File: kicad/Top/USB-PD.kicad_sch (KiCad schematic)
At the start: 43 parts

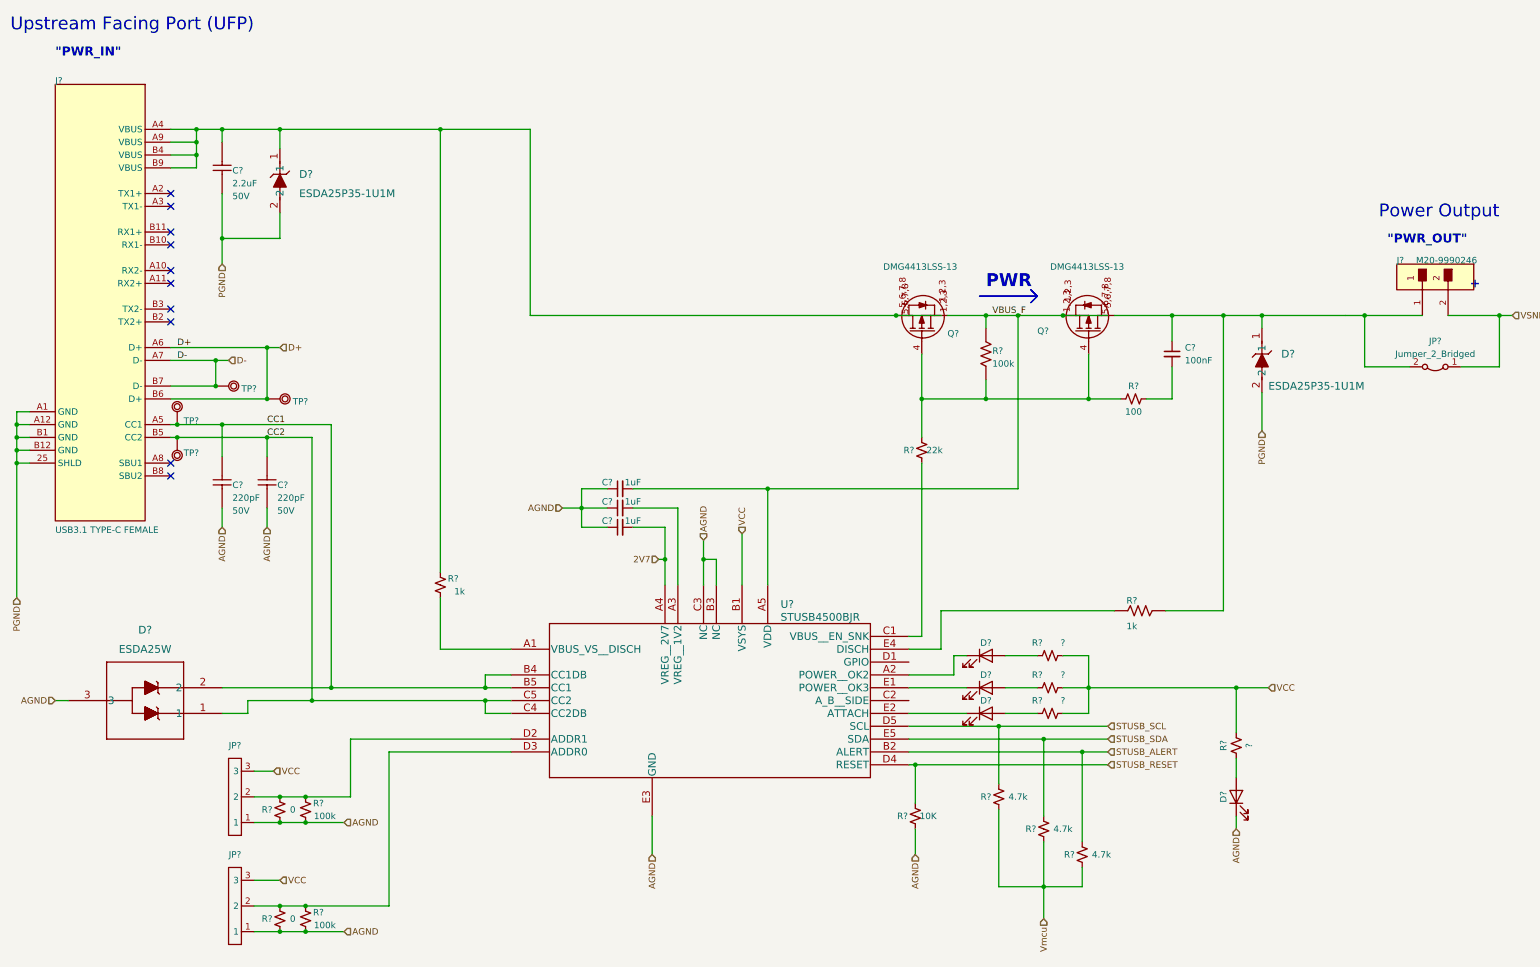
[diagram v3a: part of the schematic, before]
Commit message: Annotated USB-PD schematic
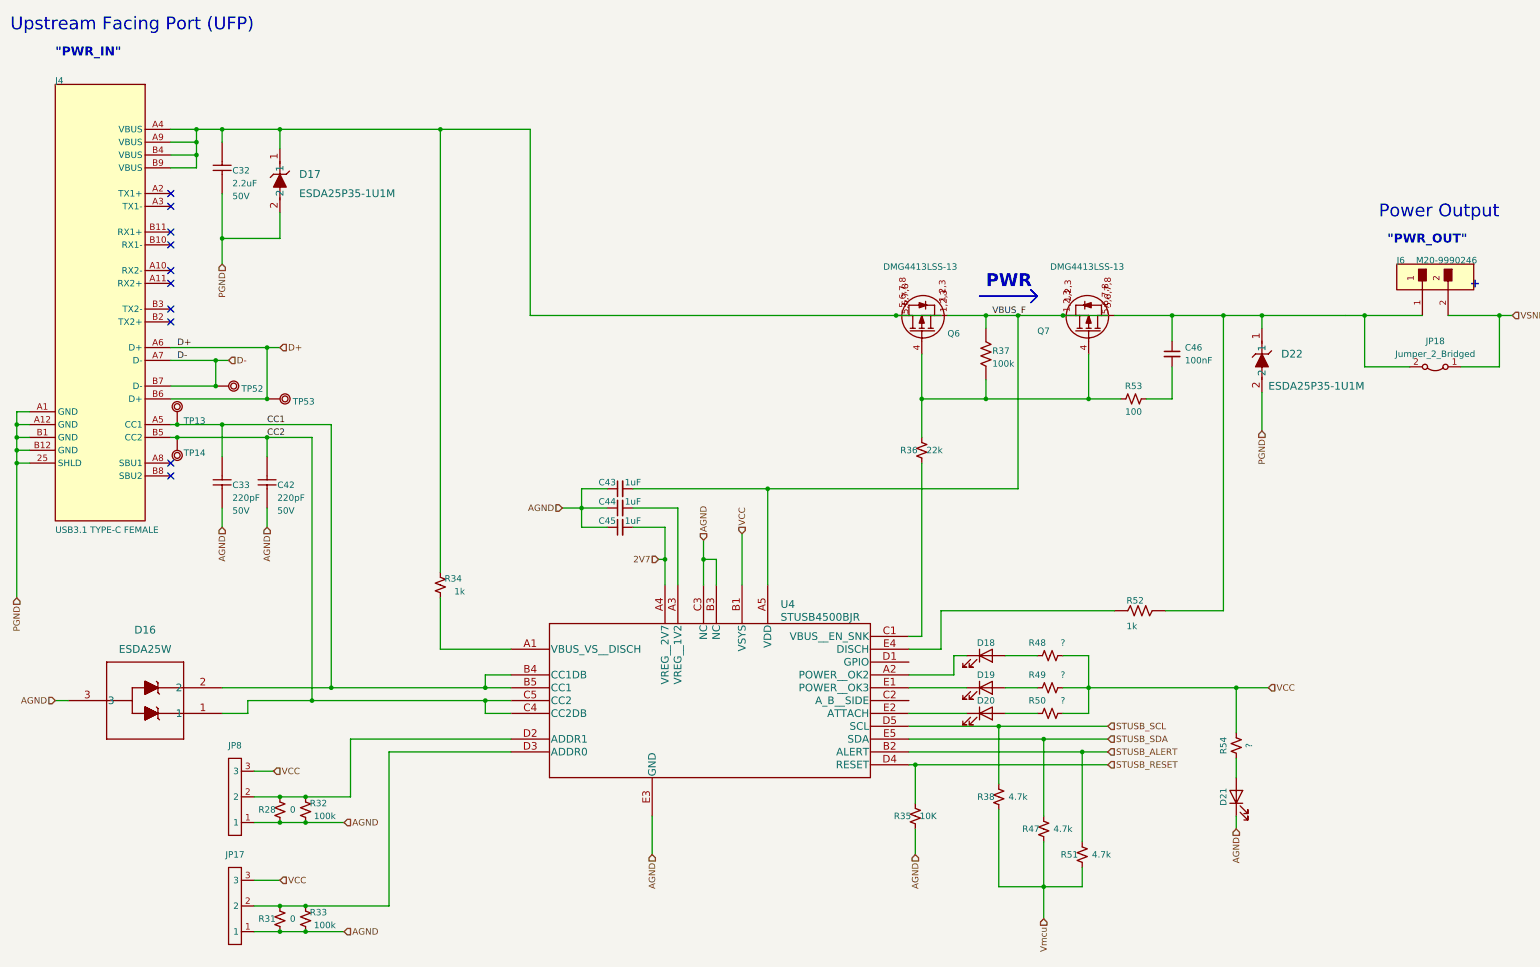
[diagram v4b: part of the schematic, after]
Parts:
- gave numbers to parts that had none: 43

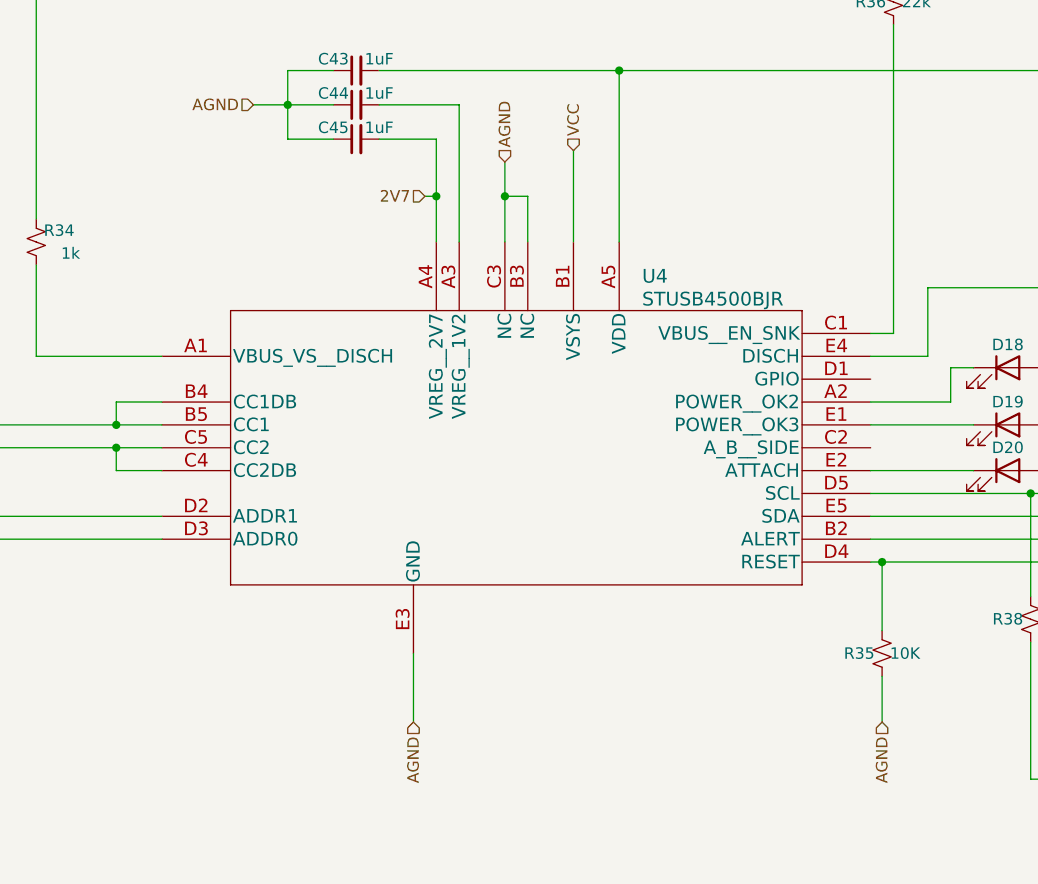
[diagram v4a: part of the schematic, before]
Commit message: Added STUSB4500QTR
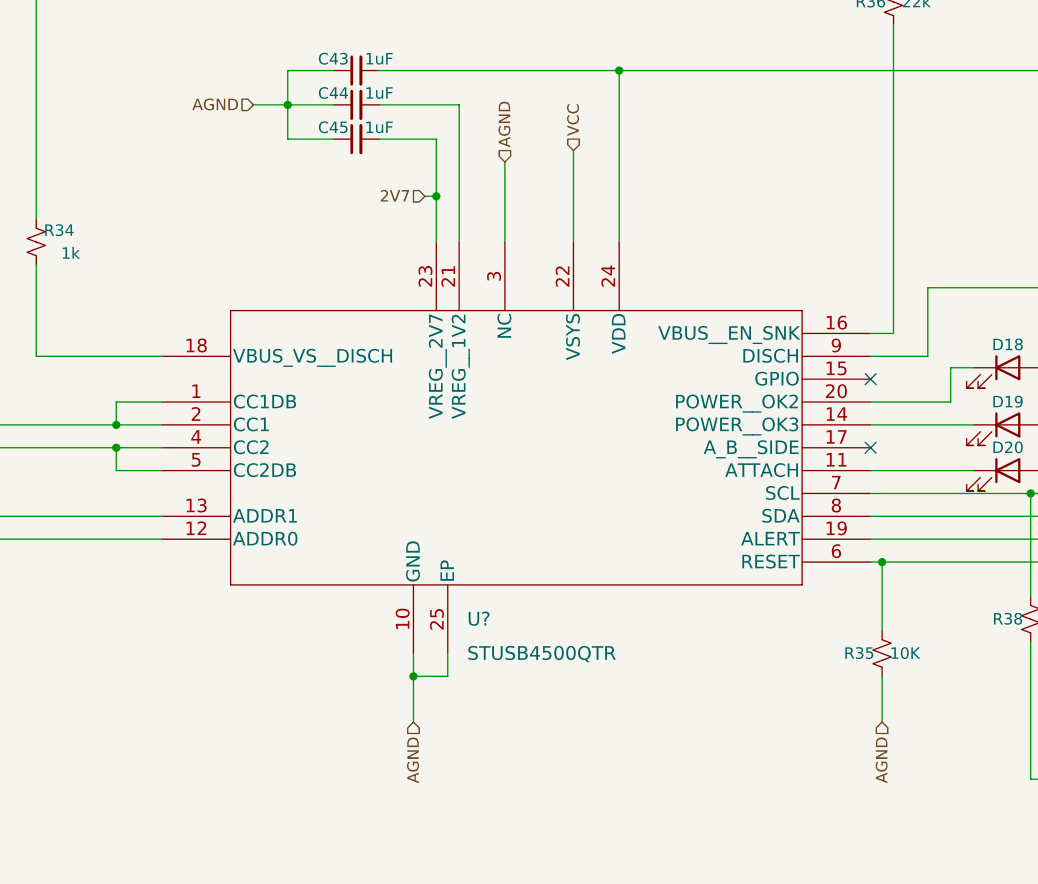
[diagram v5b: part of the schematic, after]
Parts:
- removed U4: STUSB4500BJR, custom_modules:STUSB4500BJR, symbol STUSB4500BJR:STUSB4500BJR
- added U?: STUSB4500QTR, Ultra_Librarian:QFN24EP_4X4_STM, symbol ultralibrarian:STUSB4500QTR
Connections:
- net 2V7: now also U?.23 (VREG__2V7)
- net AGND: now also U?.10 (GND), U?.25 (EP), U?.3 (NC)
- net CC1: now also U?.1 (CC1DB), U?.2 (CC1)
- net CC2: now also U?.4 (CC2), U?.5 (CC2DB)
- net STUSB_ALERT: now also U?.19 (ALERT)
- net STUSB_RESET: now also U?.6 (RESET)
- net STUSB_SCL: now also U?.7 (SCL)
- net STUSB_SDA: now also U?.8 (SDA)
- net VBUS_F: now also U?.24 (VDD)
- net VCC: now also U?.22 (VSYS)
- net at D20.1 (K): now also U?.11 (ATTACH)
- net at R34.2: now also U?.18 (VBUS_VS__DISCH)
- net at JP17.2, R31.1, R33.1: now also U?.12 (ADDR0)
- net at D18.1 (K): now also U?.20 (POWER__OK2)
- net at C44.2: now also U?.21 (VREG__1V2)
- net at R36.1: now also U?.16 (VBUS__EN_SNK)
- net at JP8.2, R28.1, R32.1: now also U?.13 (ADDR1)
- net at D19.1 (K): now also U?.14 (POWER__OK3)
- net at R52.1: now also U?.9 (DISCH)
- no-connect marks 10 -> 12
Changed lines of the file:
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@@
   (junction (at 426.72 322.58) (diameter 0) (color 0 0 0 0)
   )
-  (junction (at 521.97 386.08) (diameter 0) (color 0 0 0 0)
-  )
   (junction (at 386.08 359.41) (diameter 0) (color 0 0 0 0)
   )
@@
   )
   (junction (at 443.23 433.07) (diameter 0) (color 0 0 0 0)
+  )
+  (junction (at 511.81 439.42) (diameter 0) (color 0 0 0 0)
   )
   (junction (at 438.15 300.99) (diameter 0) (color 0 0 0 0)
@@
   (no_connect (at 416.56 369.57))
   (no_connect (at 416.56 316.23))
+  (no_connect (at 562.61 406.4))
+  (no_connect (at 562.61 414.02))
   (no_connect (at 416.56 323.85))
   (no_connect (at 416.56 331.47))
@@
     (stroke (width 0.254) (type default) (color 0 0 0 0))
   )
-  (wire (pts (xy 524.51 386.08) (xy 524.51 391.16))
-    (stroke (width 0) (type default) (color 0 0 0 0))
-  )
   (wire (pts (xy 584.2 337.82) (xy 584.2 372.11))
     (stroke (width 0) (type default) (color 0 0 0 0))
@@
     (stroke (width 0) (type default) (color 0 0 0 0))
   )
-  (wire (pts (xy 511.81 436.88) (xy 511.81 444.5))
+  (wire (pts (xy 511.81 436.88) (xy 511.81 439.42))
     (stroke (width 0) (type default) (color 0 0 0 0))
   )
@@
     (stroke (width 0) (type default) (color 0 0 0 0))
   )
+  (wire (pts (xy 511.81 439.42) (xy 515.62 439.42))
+    (stroke (width 0) (type default) (color 0 0 0 0))
+  )
   (wire (pts (xy 421.64 300.99) (xy 416.56 300.99))
     (stroke (width 0.254) (type default) (color 0 0 0 0))
@@
     (stroke (width 0.254) (type default) (color 0 0 0 0))
   )
-  (wire (pts (xy 521.97 382.27) (xy 521.97 386.08))
-    (stroke (width 0) (type default) (color 0 0 0 0))
-  )
   (wire (pts (xy 593.09 405.13) (xy 598.17 405.13))
     (stroke (width 0) (type default) (color 0 0 0 0))
@@
   )
   (wire (pts (xy 426.72 416.56) (xy 431.8 416.56))
+    (stroke (width 0) (type default) (color 0 0 0 0))
+  )
+  (wire (pts (xy 511.81 439.42) (xy 511.81 444.5))
     (stroke (width 0) (type default) (color 0 0 0 0))
   )
@@
     (stroke (width 0) (type default) (color 0 0 0 0))
   )
-  (wire (pts (xy 521.97 386.08) (xy 524.51 386.08))
-    (stroke (width 0) (type default) (color 0 0 0 0))
-  )
   (wire (pts (xy 627.38 411.48) (xy 627.38 420.37))
     (stroke (width 0) (type default) (color 0 0 0 0))
@@
   (wire (pts (xy 416.56 308.61) (xy 421.64 308.61))
     (stroke (width 0.254) (type default) (color 0 0 0 0))
+  )
+  (wire (pts (xy 515.62 439.42) (xy 515.62 436.88))
+    (stroke (width 0) (type default) (color 0 0 0 0))
   )
   (wire (pts (xy 426.72 300.99) (xy 438.15 300.99))
@@
     (stroke (width 0) (type default) (color 0 0 0 0))
   )
-  (wire (pts (xy 521.97 391.16) (xy 521.97 386.08))
+  (wire (pts (xy 521.97 382.27) (xy 521.97 391.16))
     (stroke (width 0) (type default) (color 0 0 0 0))
   )
@@
     (pin "8")
   )
-  (symbol (lib_id "STUSB4500BJR:STUSB4500BJR") (at 521.97 414.02 0) (unit 1)
-    (in_bom yes) (on_board yes)
-    (property "Reference" "U4" (id 0) (at 537.21 394.97 0)
-      (effects (font (size 1.524 1.524)) (justify left))
-    )
-    (property "Value" "STUSB4500BJR" (id 1) (at 537.21 397.51 0)
-      (effects (font (size 1.524 1.524)) (justify left))
-    )
-    (property "Footprint" "custom_modules:STUSB4500BJR" (id 2) (at 521.97 414.02 0)
-      (effects (font (size 1.524 1.524)) hide)
-    )
-    (property "Datasheet" "" (id 3) (at 562.61 406.4 0)
-      (effects (font (size 1.524 1.524)))
-    )
-    (pin "A1")
-    (pin "A2")
-    (pin "A3")
-    (pin "A4")
-    (pin "A5")
-    (pin "B1")
-    (pin "B2")
-    (pin "B3")
-    (pin "B4")
-    (pin "B5")
-    (pin "C1")
-    (pin "C2")
-    (pin "C3")
-    (pin "C4")
-    (pin "C5")
-    (pin "D1")
-    (pin "D2")
-    (pin "D3")
-    (pin "D4")
-    (pin "D5")
-    (pin "E1")
-    (pin "E2")
-    (pin "E3")
-    (pin "E4")
-    (pin "E5")
-  )
   (symbol (lib_id "Top-altium-import:1_mirrored_SI4477DY-T1-GE3") (at 570.23 345.44 0) (unit 1)
     (in_bom yes) (on_board yes)
@@
     (pin "1")
   )
+  (symbol (lib_id "ultralibrarian:STUSB4500QTR") (at 523.24 415.29 0) (unit 1)
+    (in_bom yes) (on_board yes) (fields_autoplaced)
+    (property "Reference" "U?" (id 0) (at 517.7651 433.07 0)
+      (effects (font (size 1.524 1.524)) (justify left))
+    )
+    (property "Value" "STUSB4500QTR" (id 1) (at 517.7651 436.88 0)
+      (effects (font (size 1.524 1.524)) (justify left))
+    )
+    (property "Footprint" "Ultra_Librarian:QFN24EP_4X4_STM" (id 2) (at 523.24 416.56 0)
+      (effects (font (size 1.524 1.524)) hide)
+    )
+    (property "Datasheet" "" (id 3) (at 523.24 416.56 0)
+      (effects (font (size 1.524 1.524)))
+    )
+    (pin "1")
+    (pin "10")
+    (pin "11")
+    (pin "12")
+    (pin "13")
+    (pin "14")
+    (pin "15")
+    (pin "16")
+    (pin "17")
+    (pin "18")
+    (pin "19")
+    (pin "2")
+    (pin "20")
+    (pin "21")
+    (pin "22")
+    (pin "23")
+    (pin "24")
+    (pin "25")
+    (pin "3")
+    (pin "4")
+    (pin "5")
+    (pin "6")
+    (pin "7")
+    (pin "8")
+    (pin "9")
+  )
   (symbol (lib_id "Device:LED") (at 577.85 411.48 0) (unit 1)
